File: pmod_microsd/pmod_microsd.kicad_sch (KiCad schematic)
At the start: 21 parts, among them J1 PZ254R-12-12P, J2 Micro_SD_Card_Det2, U1 AIP74LVC1T45GB236TR

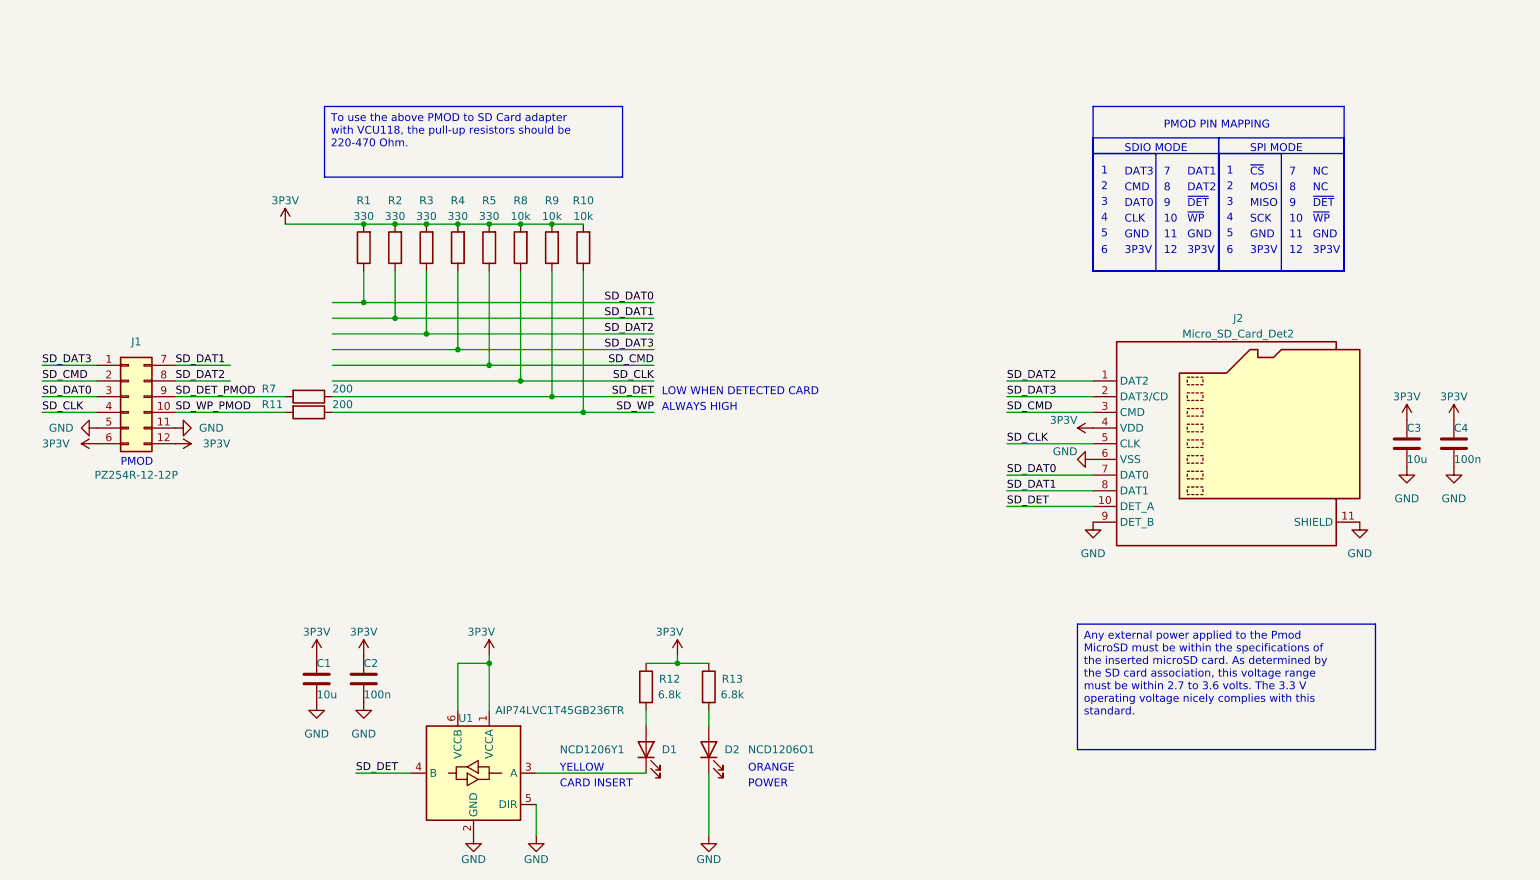
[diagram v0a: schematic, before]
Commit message: pmod_microsd: add RCLAMP0524P as ESD protection device
- Update schematic and add TVS diode for PMOD interface

Signed-off-by: Huang Rui <vowstar@gmail.com>
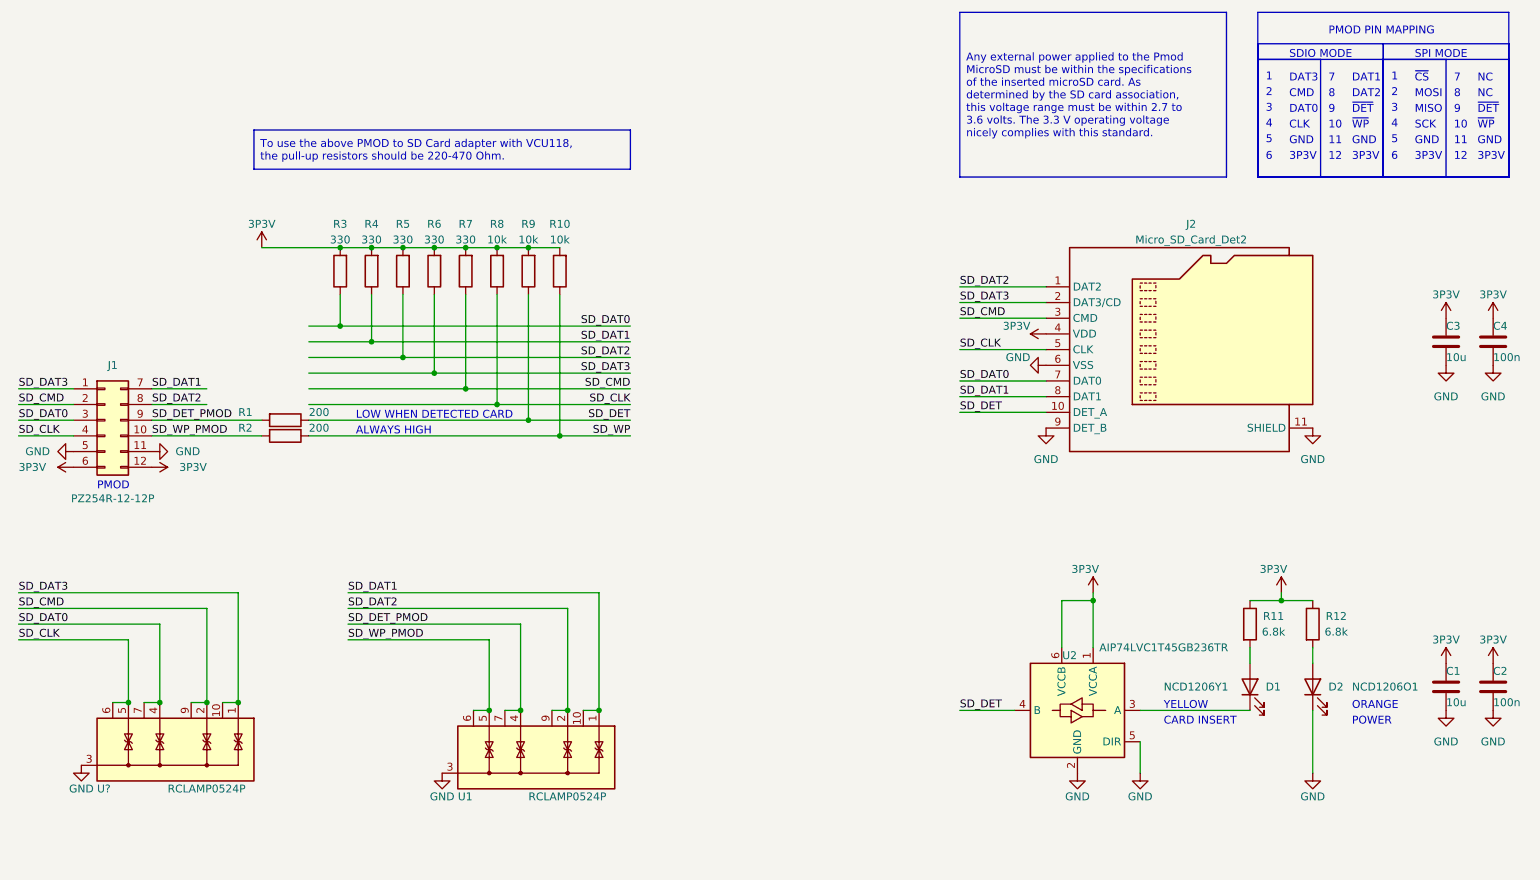
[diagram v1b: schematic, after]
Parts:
- added U1, U?: RCLAMP0524P, CHIPSAlliance_Package_SON:USON-10_2.5x1.0mm_P0.5mm, symbol CHIPSAlliance_Power_Protection:RCLAMP0524P
- renumbered R7 to R1, R12 to R11, R13 to R12, R11 to R2, R1 to R3, R2 to R4, R3 to R5, R4 to R6, R5 to R7, U1 to U2
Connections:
- net GND: now also U1.3 (G), U1.8 (G), U?.3 (G), U?.8 (G)
- net SD_CLK: now also U?.5 (IO4), U?.6 (NC)
- net SD_CMD: now also U?.2 (IO2), U?.9 (NC)
- net SD_DAT0: now also U?.4 (IO3), U?.7 (NC)
- net SD_DAT1: now also U1.1 (IO1), U1.10 (NC)
- net SD_DAT2: now also U1.2 (IO2), U1.9 (NC)
- net SD_DAT3: now also U?.1 (IO1), U?.10 (NC)
- net SD_DET_PMOD: now also U1.4 (IO3), U1.7 (NC)
- net SD_WP_PMOD: now also U1.5 (IO4), U1.6 (NC)
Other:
- moved on the sheet: C1, C2, C3, C4, D1, D2, J1, J2, R1, R10, R11, R12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

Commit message: pmod_microsd: annotate the components
- Annotate various components so that components have unique references

Signed-off-by: Huang Rui <vowstar@gmail.com>
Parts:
- gave numbers to parts that had none: 1
- renumbered C3 to C1, C1 to C2, C4 to C3, C2 to C4, U1 to U2, U2 to U3

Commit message: pmod_microsd: add PWR_FLAG to VDD and GND, ERC clean
- Add PWR_FLAG to 3P3V (VDD)
- Add PWR_FLAG to GND
- ERC Clean

Signed-off-by: Huang Rui <vowstar@gmail.com>
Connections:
- net SD_CLK: now also U2.1 (IO1), U2.10 (NC); no longer U1.5 (IO4), U1.6 (NC)
- net SD_CMD: now also U1.5 (IO4), U1.6 (NC); no longer U1.2 (IO2), U1.9 (NC)
- net SD_DAT0: now also U2.2 (IO2), U2.9 (NC); no longer U1.4 (IO3), U1.7 (NC)
- net SD_DAT1: now also U2.4 (IO3), U2.7 (NC); no longer U2.1 (IO1), U2.10 (NC)
- net SD_DAT2: now also U1.2 (IO2), U1.9 (NC); no longer U2.2 (IO2), U2.9 (NC)
- net SD_DAT3: now also U1.4 (IO3), U1.7 (NC); no longer U1.1 (IO1), U1.10 (NC)
- net SD_DET_PMOD: now also U1.1 (IO1), U1.10 (NC); no longer U2.4 (IO3), U2.7 (NC)
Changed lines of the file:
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@@
-    (effects (font (size 1.27 1.27)) (justify left bottom))
-  )
-  (label "SD_DAT1" (at 78.74 119.38 0) (fields_autoplaced)
     (effects (font (size 1.27 1.27)) (justify left bottom))
   )
   (label "SD_CLK" (at 177.8 80.01 0) (fields_autoplaced)
-    (effects (font (size 1.27 1.27)) (justify left bottom))
-  )
-  (label "SD_CMD" (at 25.4 121.92 0) (fields_autoplaced)
     (effects (font (size 1.27 1.27)) (justify left bottom))
   )
@@
     (effects (font (size 1.27 1.27)) (justify right bottom))
   )
-  (label "SD_CLK" (at 25.4 127 0) (fields_autoplaced)
+  (label "SD_DAT0" (at 78.74 121.92 0) (fields_autoplaced)
+    (effects (font (size 1.27 1.27)) (justify left bottom))
+  )
+  (label "SD_CMD" (at 25.4 127 0) (fields_autoplaced)
+    (effects (font (size 1.27 1.27)) (justify left bottom))
+  )
+  (label "SD_DAT3" (at 25.4 124.46 0) (fields_autoplaced)
     (effects (font (size 1.27 1.27)) (justify left bottom))
   )
@@
     (effects (font (size 1.27 1.27)) (justify right bottom))
   )
-  (label "SD_DAT0" (at 25.4 124.46 0) (fields_autoplaced)
-    (effects (font (size 1.27 1.27)) (justify left bottom))
-  )
-  (label "SD_DAT3" (at 25.4 119.38 0) (fields_autoplaced)
+  (label "SD_CLK" (at 78.74 119.38 0) (fields_autoplaced)
     (effects (font (size 1.27 1.27)) (justify left bottom))
   )
@@
     (effects (font (size 1.27 1.27)) (justify left bottom))
   )
+  (label "SD_DET_PMOD" (at 25.4 119.38 0) (fields_autoplaced)
+    (effects (font (size 1.27 1.27)) (justify left bottom))
+  )
   (label "SD_DET" (at 177.8 90.17 0) (fields_autoplaced)
     (effects (font (size 1.27 1.27)) (justify left bottom))
@@
     (effects (font (size 1.27 1.27)) (justify left bottom))
   )
-  (label "SD_DAT2" (at 78.74 121.92 0) (fields_autoplaced)
+  (label "SD_DAT2" (at 25.4 121.92 0) (fields_autoplaced)
     (effects (font (size 1.27 1.27)) (justify left bottom))
   )
@@
     (effects (font (size 1.27 1.27)) (justify left bottom))
   )
-  (label "SD_DET_PMOD" (at 78.74 124.46 0) (fields_autoplaced)
+  (label "SD_DAT1" (at 78.74 124.46 0) (fields_autoplaced)
     (effects (font (size 1.27 1.27)) (justify left bottom))
   )
@@
         (path "/79a75171-95fd-4fdc-a49f-40b13ef197cc"
           (reference "#PWR02") (unit 1)
+        )
+      )
+    )
+  )
+  (symbol (lib_id "CHIPSAlliance_Power:3P3V") (at 39.37 48.26 90) (unit 1)
+    (in_bom yes) (on_board yes) (dnp no)
+    (property "Reference" "#PWR025" (at 43.18 48.26 0)
+      (effects (font (size 1.27 1.27)) hide)
+    )
+    (property "Value" "3P3V" (at 35.56 48.26 90)
+      (effects (font (size 1.27 1.27)) (justify left))
+    )
+    (property "Footprint" "" (at 39.37 48.26 0)
+      (effects (font (size 1.27 1.27)) hide)
+    )
+    (property "Datasheet" "" (at 39.37 48.26 0)
+      (effects (font (size 1.27 1.27)) hide)
+    )
+    (pin "1")
+    (instances
+      (project "pmod_microsd"
+        (path "/0959ba5b-cfb3-4101-b57a-b405f558c0e6"
+          (reference "#PWR025") (unit 1)
+        )
+      )
+      (project "fmc_usb_gpio_spi_jtag"
+        (path "/387bfcf1-ae49-4b85-be89-3bb02ce2e960/9cd800a1-5b4a-4dab-b708-f8f78f4f7813"
+          (reference "#PWR0228") (unit 1)
         )
       )
@@
     )
   )
+  (symbol (lib_id "power:PWR_FLAG") (at 39.37 53.34 0) (unit 1)
+    (in_bom yes) (on_board yes) (dnp no)
+    (property "Reference" "#FLG02" (at 39.37 51.435 0)
+      (effects (font (size 1.27 1.27)) hide)
+    )
+    (property "Value" "PWR_FLAG" (at 35.56 50.8 0)
+      (effects (font (size 1.27 1.27)) (justify right))
+    )
+    (property "Footprint" "" (at 39.37 53.34 0)
+      (effects (font (size 1.27 1.27)) hide)
+    )
+    (property "Datasheet" "~" (at 39.37 53.34 0)
+      (effects (font (size 1.27 1.27)) hide)
+    )
+    (pin "1")
+    (instances
+      (project "pmod_microsd"
+        (path "/0959ba5b-cfb3-4101-b57a-b405f558c0e6"
+          (reference "#FLG02") (unit 1)
+        )
+      )
+      (project "fmc_usb_gpio_spi_jtag"
+        (path "/387bfcf1-ae49-4b85-be89-3bb02ce2e960/9cd800a1-5b4a-4dab-b708-f8f78f4f7813"
+          (reference "#FLG06") (unit 1)
+        )
+      )
+    )
+  )
   (symbol (lib_id "Device:R") (at 97.79 67.31 180) (unit 1)
     (in_bom yes) (on_board yes) (dnp no)
@@
         (path "/387bfcf1-ae49-4b85-be89-3bb02ce2e960/ee2d37c4-eb99-4eca-94f7-bc755b7135e3"
           (reference "#PWR0189") (unit 1)
+        )
+      )
+    )
+  )
+  (symbol (lib_id "CHIPSAlliance_Power:GND") (at 39.37 53.34 270) (unit 1)
+    (in_bom yes) (on_board yes) (dnp no)
+    (property "Reference" "#PWR026" (at 33.02 53.34 0)
+      (effects (font (size 1.27 1.27)) hide)
+    )
+    (property "Value" "GND" (at 35.56 53.34 90)
+      (effects (font (size 1.27 1.27)) (justify right))
+    )
+    (property "Footprint" "" (at 39.37 53.34 0)
+      (effects (font (size 1.27 1.27)) hide)
+    )
+    (property "Datasheet" "" (at 39.37 53.34 0)
+      (effects (font (size 1.27 1.27)) hide)
+    )
+    (pin "1")
+    (instances
+      (project "pmod_microsd"
+        (path "/0959ba5b-cfb3-4101-b57a-b405f558c0e6"
+          (reference "#PWR026") (unit 1)
+        )
+      )
+      (project "fmc_usb_gpio_spi_jtag"
+        (path "/387bfcf1-ae49-4b85-be89-3bb02ce2e960/4338fda8-0ea2-4bf2-b1c2-c685ef11d6a0"
+          (reference "#PWR078") (unit 1)
+        )
+        (path "/387bfcf1-ae49-4b85-be89-3bb02ce2e960/9cd800a1-5b4a-4dab-b708-f8f78f4f7813"
+          (reference "#PWR0259") (unit 1)
         )
       )
@@
         )
       )
+    )
+  )
+  (symbol (lib_id "power:PWR_FLAG") (at 39.37 48.26 0) (unit 1)
+    (in_bom yes) (on_board yes) (dnp no)
+    (property "Reference" "#FLG01" (at 39.37 46.355 0)
+      (effects (font (size 1.27 1.27)) hide)
+    )
+    (property "Value" "PWR_FLAG" (at 35.56 45.72 0)
+      (effects (font (size 1.27 1.27)) (justify right))
+    )
+    (property "Footprint" "" (at 39.37 48.26 0)
+      (effects (font (size 1.27 1.27)) hide)
+    )
+    (property "Datasheet" "~" (at 39.37 48.26 0)
+      (effects (font (size 1.27 1.27)) hide)
+    )
+    (pin "1")
+    (instances
+      (project "pmod_microsd"
+        (path "/0959ba5b-cfb3-4101-b57a-b405f558c0e6"
+          (reference "#FLG01") (unit 1)
+        )
+      )
+      (project "fmc_usb_gpio_spi_jtag"
+        (path "/387bfcf1-ae49-4b85-be89-3bb02ce2e960/9cd800a1-5b4a-4dab-b708-f8f78f4f7813"
+          (reference "#FLG04") (unit 1)
+        )
+      )

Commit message: pmod_microsd: Migrate to kicad8
- Migrate schematics to kicad8
- Migrate PCB to kicad8
- Clean ERC
- Clean LVS and DRC

Signed-off-by: Huang Rui <vowstar@gmail.com>
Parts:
- U3: footprint Package_TO_SOT_SMD:SOT-23-6 -> CHIPSAlliance_Package_TO_SOT_SMD:SOT-23-6
